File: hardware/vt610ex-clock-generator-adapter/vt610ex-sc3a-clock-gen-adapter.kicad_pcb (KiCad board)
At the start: 2 copper layers, 20.2 x 12 mm, 10 parts, among them J11 Conn_01x01_Pin, J12 Conn_01x01_Pin, J21 Conn_01x01_Pin, J22 Conn_01x01_Pin, J30 Conn_01x03_Pin

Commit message: Resolve "PCBway Compatible Gerbers"
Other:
- board text added: "${fab-jlc}"
- board text removed: "JLCJLCJLCJLC"
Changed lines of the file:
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@@
   (title_block
     (title "${proj-title}")
-    (date "2023-09-16")
+    (date "2023-11-25")
     (rev "${proj-version}")
     (company "${proj-author}")
@@
     )
   )
+  (property "fab-jlc" "JLCJLCJLCJLC")
+  (property "fab-pcbway" "WayWayWay")
   (property "proj-author" "Rene Wolf")
   (property "proj-license" "CC BY-SA 4.0")
   (property "proj-title" "cxadc clock-gen adapter")
-  (property "proj-version" "B")
+  (property "proj-version" "C")
   (net 0 "")
   (net 1 "Net-(J30-Pin_2)")
@@
     (property "ki_keywords" "connector")
     (attr smd)
-    (fp_text reference "J30" (at -7.112 0 unlocked) (layer "F.SilkS") hide
-        (effects (font (size 1 1) (thickness 0.1)))
+    (fp_text reference "J30" (at -2.3 4.8 unlocked) (layer "F.SilkS")
+        (effects (font (size 1 1) (thickness 0.15)))
     )
     (fp_text value "Conn_01x03_Pin" (at 0 6.604 unlocked) (layer "F.Fab")
@@
     (effects (font (size 1 0.9) (thickness 0.15)) (justify left bottom mirror))
   )
-  (gr_text "Rev ${REVISION}" (at 139.8 86.35) (layer "F.SilkS")
+  (gr_text "Rev ${REVISION}" (at 129.4 86.6) (layer "F.SilkS")
     (effects (font (size 1 1) (thickness 0.15)) (justify left bottom))
   )
@@
     (effects (font (size 1 1) (thickness 0.15)) (justify bottom))
   )
-  (gr_text "JLCJLCJLCJLC" (at 134.1 76.8) (layer "F.SilkS")
-    (effects (font (size 1 1) (thickness 0.15)) (justify left bottom))
+  (gr_text "${fab-jlc}" (at 139.4 76) (layer "F.SilkS")
+    (effects (font (size 1 1) (thickness 0.15)))
   )
   (gr_text "GND" (at 126.5 77.2 90) (layer "F.SilkS")
@@
   (via (at 138.9 79.7) (size 0.8) (drill 0.4) (layers "F.Cu" "B.Cu") (free) (net 4))
   (via (at 129.5 79.2) (size 0.8) (drill 0.4) (layers "F.Cu" "B.Cu") (free) (net 4))
-  (via (at 131.5 85.1) (size 0.8) (drill 0.4) (layers "F.Cu" "B.Cu") (free) (net 4))
+  (via (at 131.5 84.8) (size 0.8) (drill 0.4) (layers "F.Cu" "B.Cu") (free) (net 4))
   (segment (start 135.2 78.1) (end 131.6 78.1) (width 0.25) (layer "F.Cu") (net 5))
   (zone (net 4) (net_name "GND") (layer "F.Cu") (hatch edge 0.5)

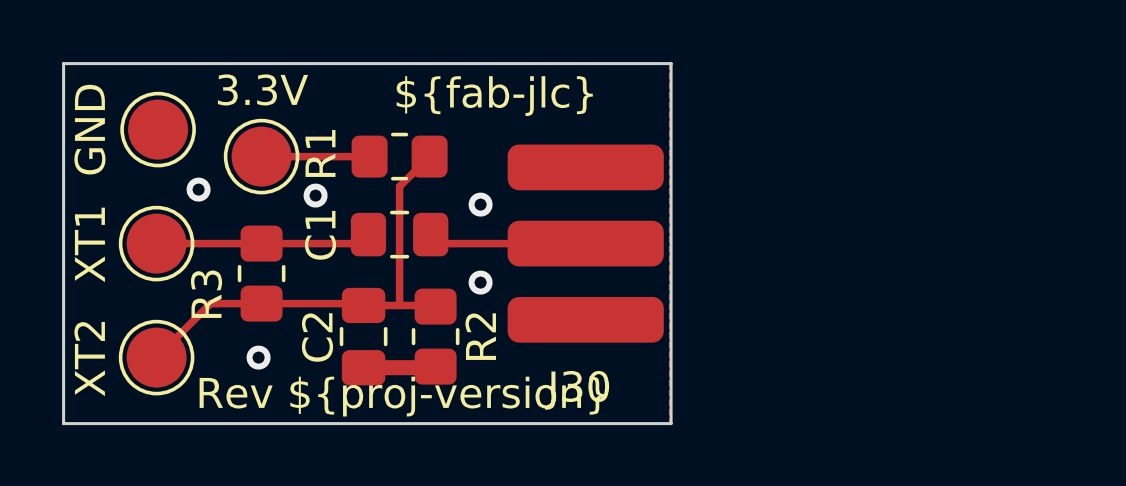
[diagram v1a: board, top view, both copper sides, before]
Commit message: Resolve "Extend build guide to explain SMA connectors for clock lines"
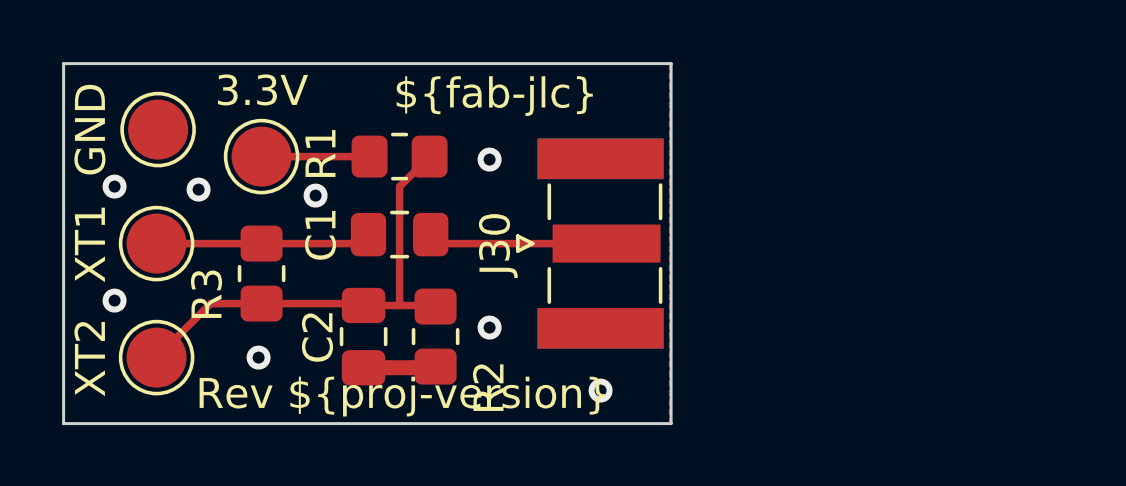
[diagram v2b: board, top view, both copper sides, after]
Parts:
- J30: value Conn_01x03_Pin -> Conn_Coaxial; footprint custom-vt610ex-sc3a:PinHeader_1x03_P2.54mm_Edge -> Connector_Coaxial:SMA_Samtec_SMA-J-P-X-ST-EM1_EdgeMount
- moved J30 1.60 mm to (142.9, 81.0), turned to 90 degrees
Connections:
- C1 pad 1: Net-(J30-Pin_2) -> Net-(J30-In)
- J30 pad 1: GND -> Net-(J30-In)
- J30 pad 2: Net-(J30-Pin_2) -> GND
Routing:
- net Net-(J30-Pin_2): track 5.04 -> 0.00 mm
- net Net-(J30-In): track 0.00 -> 5.04 mm
- net GND: vias 5 -> 8
